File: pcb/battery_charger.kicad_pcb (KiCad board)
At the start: 2 copper layers, 36.2 x 24.2 mm, 20 parts, among them J1 USB_B_Micro, J2 IN+, J3 IN-, J4 OUT+, J5 BAT+, J6 BAT-, J7 OUT-, U1 TP4056, U2 DW01A, U3 FS8205A

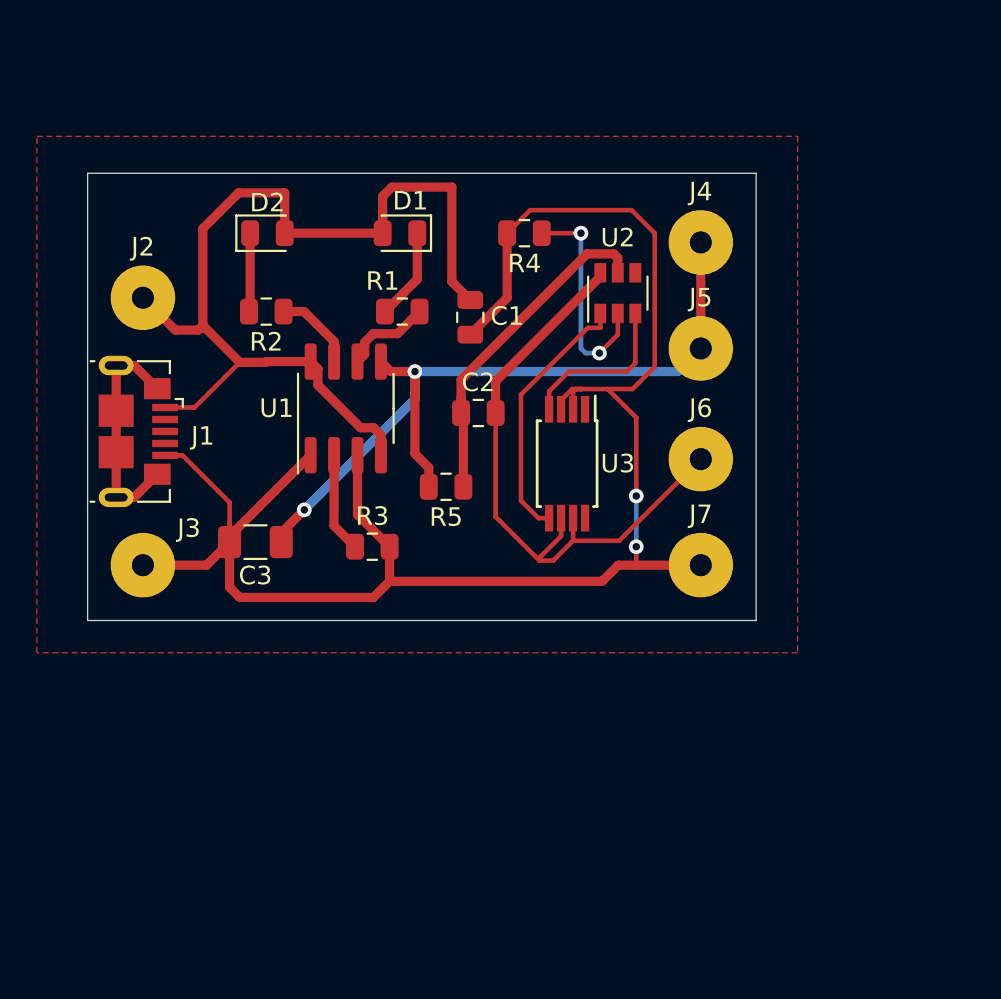
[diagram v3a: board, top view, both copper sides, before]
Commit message: Se acomodan conectores y se cambian referencias en pcb
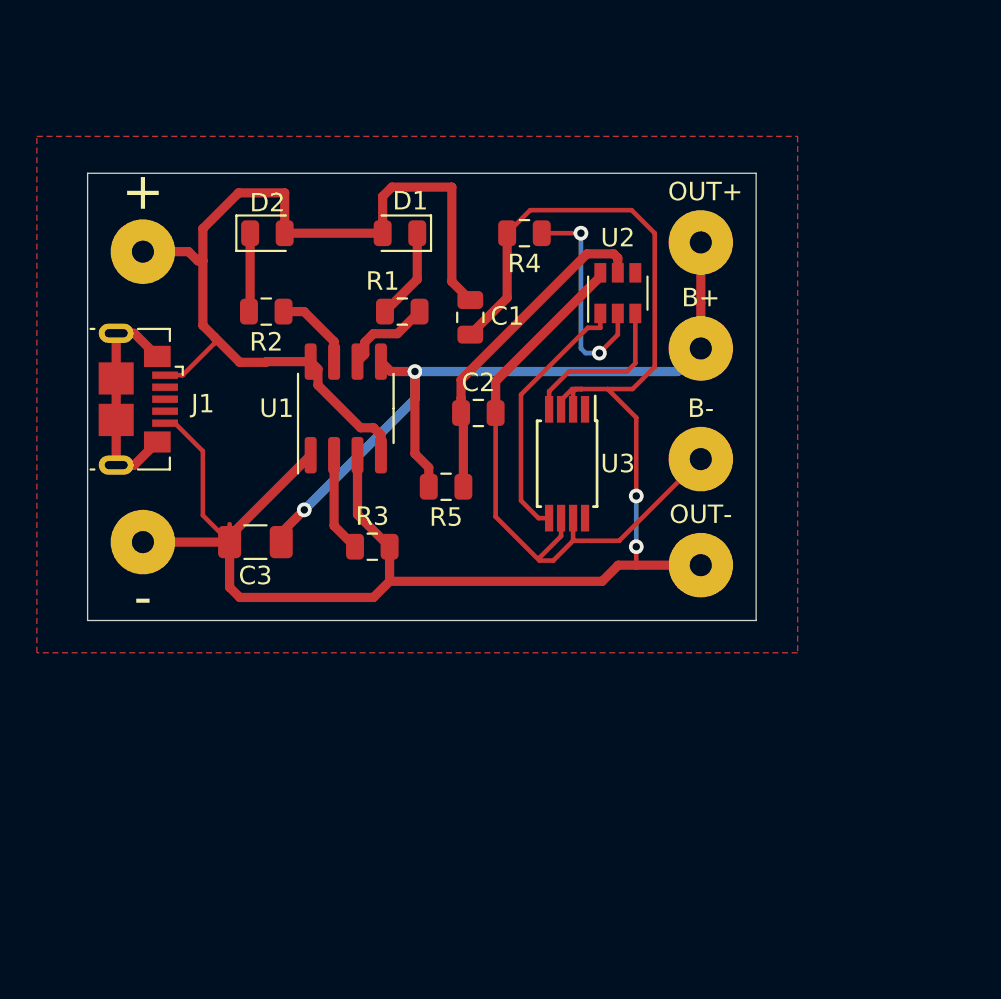
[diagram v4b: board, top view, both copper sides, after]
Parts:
- removed J2: IN+, Connector_Wire:SolderWirePad_1x01_Drill1.2mm
- removed J4: OUT+, Connector_Wire:SolderWirePad_1x01_Drill1.2mm
- added +: IN+, Connector_Wire:SolderWirePad_1x01_Drill1.2mm, F.Cu at (105.5, 121.5)
- added OUT+: OUT+, Connector_Wire:SolderWirePad_1x01_Drill1.2mm, F.Cu at (135.8, 121.0)
- moved J1 1.75 mm to (105.2, 129.5)
- moved - 1.25 mm to (105.5, 137.2)
- renumbered J3 to -, J5 to B+, J6 to B-, J7 to OUT-
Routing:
- net GND: track 95.6 -> 97.6 mm
- net +5V: track 53.4 -> 51.4 mm
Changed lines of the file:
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@@
     (thickness 1.6)
     (drawings 4)
-    (tracks 142)
+    (tracks 145)
     (zones 0)
     (modules 20)
@@
   )
   (module Connector_USB:USB_Micro-B_GCT_USB3076-30-A (layer F.Cu)
-    (at 105.25 131.25 270)
+    (at 105.25 129.5 270)
     (descr "GCT Micro USB https://gct.co/files/drawings/usb3076.pdf")
     (tags "Micro-USB SMD Typ-B GCT")
@@
     (tags connector)
     (attr virtual)
-    (fp_text reference J7 (at 0 -2.75) (layer F.SilkS)
+    (fp_text reference OUT- (at 0 -2.75) (layer F.SilkS)
       (effects (font (size 1 1) (thickness 0.15)))
     )
@@
     (tags connector)
     (attr virtual)
-    (fp_text reference J6 (at 0 -2.75) (layer F.SilkS)
+    (fp_text reference B- (at 0 -2.75) (layer F.SilkS)
       (effects (font (size 1 1) (thickness 0.15)))
     )
@@
     (tags connector)
     (attr virtual)
-    (fp_text reference J5 (at 0 -2.75) (layer F.SilkS)
+    (fp_text reference B+ (at 0 -2.75) (layer F.SilkS)
       (effects (font (size 1 1) (thickness 0.15)))
     )
@@
     (tags connector)
     (attr virtual)
-    (fp_text reference J4 (at 0 -2.75) (layer F.SilkS)
+    (fp_text reference OUT+ (at 0.25 -2.75) (layer F.SilkS)
       (effects (font (size 1 1) (thickness 0.15)))
     )
@@
   )
   (module Connector_Wire:SolderWirePad_1x01_Drill1.2mm (layer F.Cu)
-    (at 105.5 138.5)
+    (at 105.5 137.25)
     (descr "Wire solder connection")
     (tags connector)
     (attr virtual)
-    (fp_text reference J3 (at 2.5 -2) (layer F.SilkS)
-      (effects (font (size 1 1) (thickness 0.15)))
+    (fp_text reference - (at 0 3) (layer F.SilkS)
+      (effects (font (size 2 2) (thickness 0.15)))
     )
     (fp_text value IN- (at 0 3.175) (layer F.Fab)
@@
   )
   (module Connector_Wire:SolderWirePad_1x01_Drill1.2mm (layer F.Cu)
-    (at 105.5 124)
+    (at 105.5 121.5)
     (descr "Wire solder connection")
     (tags connector)
     (attr virtual)
-    (fp_text reference J2 (at 0 -2.75) (layer F.SilkS)
-      (effects (font (size 1 1) (thickness 0.15)))
+    (fp_text reference + (at 0 -3.25) (layer F.SilkS)
+      (effects (font (size 2 2) (thickness 0.15)))
     )
     (fp_text value IN+ (at 0 3.175) (layer F.Fab)
@@
   (segment (start 114.595 127.4625) (end 112.210662 127.4625) (width 0.5) (layer F.Cu) (net 1))
   (segment (start 112.173162 127.5) (end 110.75 127.5) (width 0.5) (layer F.Cu) (net 1))
-  (segment (start 110.75 127.5) (end 108.75 125.5) (width 0.5) (layer F.Cu) (net 1))
   (segment (start 122.25 123.125) (end 123.25 124.125) (width 0.5) (layer F.Cu) (net 1))
   (segment (start 122.25 118) (end 122.25 123.125) (width 0.5) (layer F.Cu) (net 1))
@@
   (segment (start 113.1875 120.5) (end 113.1875 118.3125) (width 0.5) (layer F.Cu) (net 1))
   (segment (start 110.6875 118.3125) (end 108.75 120.25) (width 0.5) (layer F.Cu) (net 1))
-  (segment (start 108.75 120.25) (end 108.75 125.5) (width 0.5) (layer F.Cu) (net 1))
   (segment (start 113.1875 118.3125) (end 110.6875 118.3125) (width 0.5) (layer F.Cu) (net 1))
-  (segment (start 108.499941 125.750059) (end 108.75 125.5) (width 0.5) (layer F.Cu) (net 1))
-  (segment (start 107.250059 125.750059) (end 108.499941 125.750059) (width 0.5) (layer F.Cu) (net 1))
-  (segment (start 105.5 124) (end 107.250059 125.750059) (width 0.5) (layer F.Cu) (net 1))
-  (segment (start 108.3 129.95) (end 110.75 127.5) (width 0.25) (layer F.Cu) (net 1))
-  (segment (start 106.7 129.95) (end 108.3 129.95) (width 0.25) (layer F.Cu) (net 1))
+  (segment (start 107.974958 121.5) (end 108.474958 122) (width 0.5) (layer F.Cu) (net 1))
+  (segment (start 108.474958 122) (end 108.75 122) (width 0.5) (layer F.Cu) (net 1))
+  (segment (start 105.5 121.5) (end 107.974958 121.5) (width 0.5) (layer F.Cu) (net 1))
+  (segment (start 108.75 120.25) (end 108.75 122) (width 0.5) (layer F.Cu) (net 1))
+  (segment (start 108.75 122) (end 108.75 125.5) (width 0.5) (layer F.Cu) (net 1))
+  (segment (start 109.375 126.475) (end 109.375 126.125) (width 0.25) (layer F.Cu) (net 1))
+  (segment (start 107.65 128.2) (end 109.375 126.475) (width 0.25) (layer F.Cu) (net 1))
+  (segment (start 106.7 128.2) (end 107.65 128.2) (width 0.25) (layer F.Cu) (net 1))
+  (segment (start 110.75 127.5) (end 109.375 126.125) (width 0.5) (layer F.Cu) (net 1))
+  (segment (start 109.375 126.125) (end 108.75 125.5) (width 0.5) (layer F.Cu) (net 1))
   (segment (start 117.135 135.76) (end 117.135 132.5375) (width 0.5) (layer F.Cu) (net 2))
   (segment (start 118.875 137.5) (end 117.135 135.76) (width 0.5) (layer F.Cu) (net 2))
@@
   (segment (start 110.75 140.25) (end 110.2 139.7) (width 0.5) (layer F.Cu) (net 2))
   (segment (start 130.400002 139.375) (end 118.875 139.375) (width 0.5) (layer F.Cu) (net 2))
-  (segment (start 108.95 138.5) (end 110.2 137.25) (width 0.5) (layer F.Cu) (net 2))
-  (segment (start 105.5 138.5) (end 108.95 138.5) (width 0.5) (layer F.Cu) (net 2))
   (segment (start 110.2 136.275) (end 110.2 137.25) (width 0.25) (layer F.Cu) (net 2))
-  (segment (start 110.2 135.1) (end 110.2 136.275) (width 0.25) (layer F.Cu) (net 2))
-  (segment (start 107.65 132.55) (end 110.2 135.1) (width 0.25) (layer F.Cu) (net 2))
-  (segment (start 106.7 132.55) (end 107.65 132.55) (width 0.25) (layer F.Cu) (net 2))
   (segment (start 130.400002 139.375) (end 131.275002 138.5) (width 0.5) (layer F.Cu) (net 2))
   (segment (start 128.825 130.05) (end 128.825 129.074998) (width 0.25) (layer F.Cu) (net 2))
@@
   (segment (start 130.699999 128.949999) (end 132.050001 128.949999) (width 0.25) (layer F.Cu) (net 2))
   (segment (start 132.050001 128.949999) (end 133.25 127.75) (width 0.25) (layer F.Cu) (net 2))
+  (segment (start 105.5 137.25) (end 110.2 137.25) (width 0.5) (layer F.Cu) (net 2))
+  (segment (start 107.235002 130.8) (end 108.75 132.314998) (width 0.25) (layer F.Cu) (net 2))
+  (segment (start 106.7 130.8) (end 107.235002 130.8) (width 0.25) (layer F.Cu) (net 2))
+  (segment (start 108.75 135.8) (end 110.2 137.25) (width 0.25) (layer F.Cu) (net 2))
+  (segment (start 108.75 132.314998) (end 108.75 135.8) (width 0.25) (layer F.Cu) (net 2))
   (segment (start 124.625 129.45) (end 124.625 130.25) (width 0.5) (layer F.Cu) (net 3))
   (segment (start 124.625 128.53) (end 124.625 129.45) (width 0.5) (layer F.Cu) (net 3))
@@
   (segment (start 111.3125 124.6875) (end 111.25 124.75) (width 0.5) (layer F.Cu) (net 7))
   (segment (start 111.3125 120.5) (end 111.3125 124.6875) (width 0.5) (layer F.Cu) (net 7))
-  (segment (start 104.05 134.825) (end 104.05 132.375) (width 0.5) (layer F.Cu) (net 8))
-  (segment (start 104.05 130.125) (end 104.05 127.675) (width 0.5) (layer F.Cu) (net 8))
-  (segment (start 105.025 127.675) (end 106.28 128.93) (width 0.5) (layer F.Cu) (net 8))
-  (segment (start 104.05 127.675) (end 105.025 127.675) (width 0.5) (layer F.Cu) (net 8))
-  (segment (start 105.025 134.825) (end 106.28 133.57) (width 0.5) (layer F.Cu) (net 8))
-  (segment (start 104.05 134.825) (end 105.025 134.825) (width 0.5) (layer F.Cu) (net 8))
-  (segment (start 104.05 132.375) (end 104.05 130.125) (width 0.5) (layer F.Cu) (net 8))
+  (segment (start 104.05 128.375) (end 104.05 125.925) (width 0.5) (layer F.Cu) (net 8))
+  (segment (start 104.05 130.625) (end 104.05 128.375) (width 0.5) (layer F.Cu) (net 8))
+  (segment (start 104.05 133.075) (end 104.05 130.625) (width 0.5) (layer F.Cu) (net 8))
+  (segment (start 105.025 125.925) (end 106.28 127.18) (width 0.5) (layer F.Cu) (net 8))
+  (segment (start 104.05 125.925) (end 105.025 125.925) (width 0.5) (layer F.Cu) (net 8))
+  (segment (start 105.025 133.075) (end 106.28 131.82) (width 0.5) (layer F.Cu) (net 8))
+  (segment (start 104.05 133.075) (end 105.025 133.075) (width 0.5) (layer F.Cu) (net 8))
   (segment (start 117.53071 126.412358) (end 117.53071 127.06679) (width 0.5) (layer F.Cu) (net 12))
   (segment (start 117.53071 127.06679) (end 117.135 127.4625) (width 0.5) (layer F.Cu) (net 12))

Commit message: Se agregan modelos 3D
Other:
- board text added: "Battery Charger"
- board text added: "Designed in Argentina"
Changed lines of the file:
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@@
   (general
     (thickness 1.6)
-    (drawings 4)
+    (drawings 6)
     (tracks 145)
     (zones 0)
@@
       (rotate (xyz 0 0 0))
     )
+    (model ${KISYS3DMOD}/Connector_USB.3dshapes/USB_Micro-B_Molex_47346-0001.wrl
+      (at (xyz 0 0 0))
+      (scale (xyz 1 1 1))
+      (rotate (xyz 0 0 0))
+    )
   )
   (module Package_SO:TSSOP-8_4.4x3mm_P0.65mm (layer F.Cu)
@@
       (rotate (xyz 0 0 0))
     )
+    (model ${KISYS3DMOD}/Package_SO.3dshapes/SSOP-8_3.95x5.21x3.27mm_P1.27mm.step
+      (at (xyz 0 0 0))
+      (scale (xyz 1 1 1))
+      (rotate (xyz 0 0 0))
+    )
   )
   (module Resistor_SMD:R_0805_2012Metric (layer F.Cu)
@@
     )
   )
+  (gr_text "Designed\nin\nArgentina" (at 111 133) (layer F.SilkS)
+    (effects (font (size 0.7 0.7) (thickness 0.1)))
+  )
+  (gr_text "Battery Charger" (at 127 140) (layer F.SilkS)
+    (effects (font (size 1 1) (thickness 0.15)))
+  )
   (gr_line (start 102.5 141.5) (end 102.5 117.25) (layer Edge.Cuts) (width 0.05))
